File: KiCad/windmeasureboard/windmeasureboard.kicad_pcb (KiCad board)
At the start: 2 copper layers, 101.2 x 73.2 mm, 29 parts, among them J1 ESQ-120-XX-X-D-XX, U1 ESP32-S2-DEVKITC-1, U2 LM1084ISX-5.0_NOPB, U3 INA229AIDGSR, U4 INA229AIDGSR, U5 INA229AIDGSR, U6 INA229AIDGSR, U7 INA229AIDGSR, U8 INA229AIDGSR, U9 INA229AIDGSR

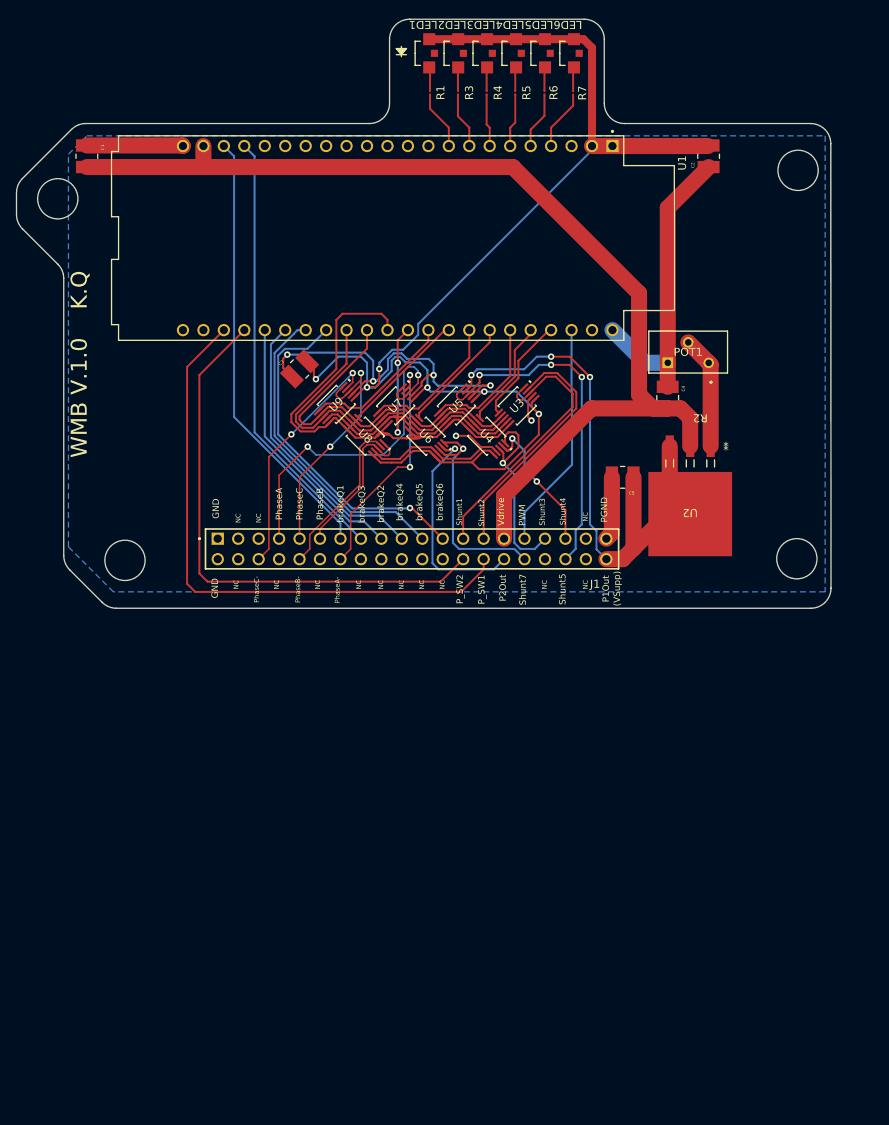
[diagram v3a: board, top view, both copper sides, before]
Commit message: started V2 WMB
fixed PSU issue
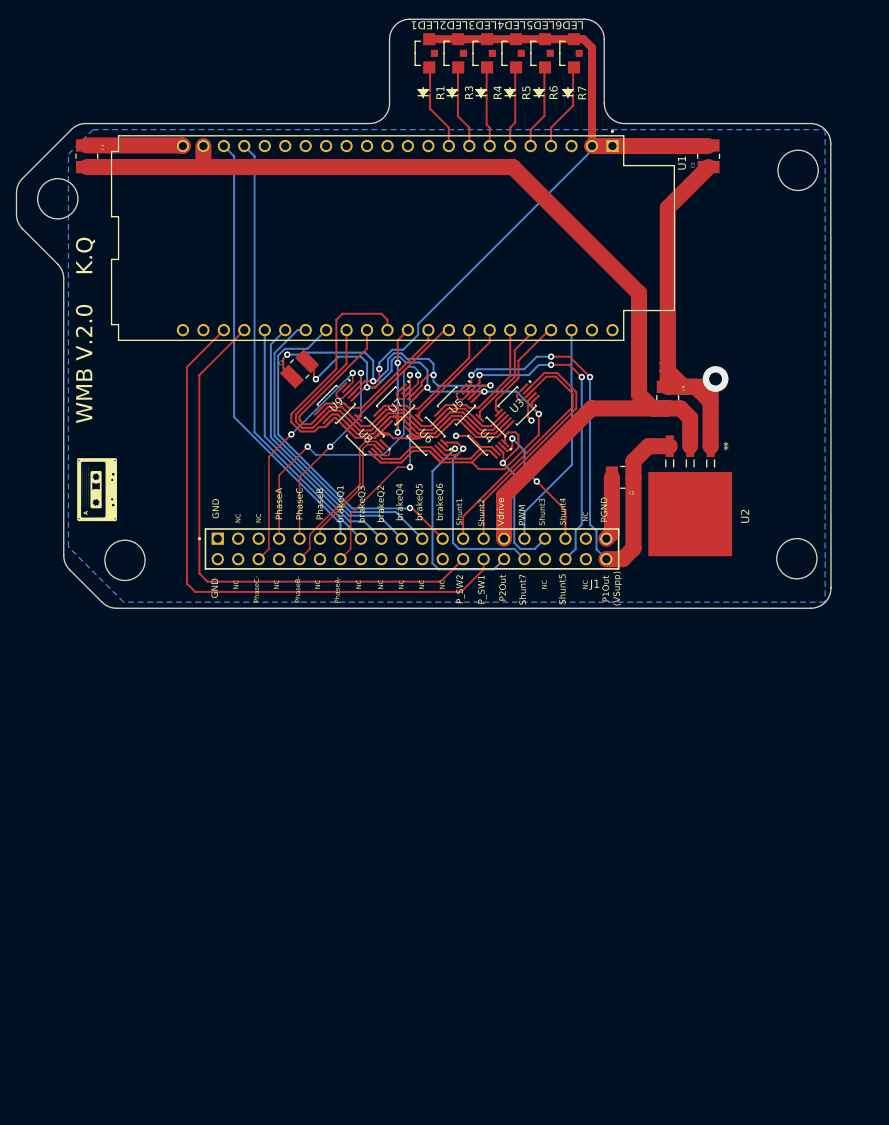
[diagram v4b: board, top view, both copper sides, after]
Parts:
- removed POT1: 3296Y-1-502LF, footprints:POT_3296Y
- removed R2: CRCW04021K00FKED, footprints:RES_CRCW_0402
- added G***: LOGO, LOGO, F.Cu at (91.2, 78.7)
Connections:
- U2 pad 1: Net-(U2-ADJ/GND) -> GND
- U2 pad 4: Shunt6 -> unconnected-(U2-Pad4)
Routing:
- net Net-(U2-ADJ/GND): track 14.0 -> 0.00 mm
- net GND: track 130.7 -> 144.0 mm, vias 6 -> 7
- net Shunt6: track 73.4 -> 62.4 mm
- net unconnected-(U2-Pad4): track 0.00 -> 6.37 mm
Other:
- board text added: "WMB V.2.0 K.Q"
- board text removed: "WMB V.1.0 K.Q"

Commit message: Finished WMB V2.1
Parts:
- removed R7: ERJXGNJ560Y, footprints:ERJXGN_RCD
- added R2: CPA2512E56R0FS-T10, footprints:RESC6332X80N, F.Cu at (134.9, 66.7)
- R1, R3, R4, R5, R6: value ERJXGNJ560Y -> CPA2512E56R0FS-T10; footprint footprints:ERJXGN_RCD -> footprints:RESC6332X80N
- moved C5 45.8 mm to (161.6, 122.7)
- moved C3 45.8 mm to (121.5, 109.3)
- moved C4 45.8 mm to (167.2, 112.8)
- moved G*** 45.8 mm to (96.4, 124.3)
- moved J1 45.8 mm to (135.5, 131.6)
- moved U2 45.8 mm to (170.0, 127.1)
- moved U3 45.8 mm to (148.5, 113.9)
- moved U4 45.8 mm to (144.8, 117.6)
- moved U5 45.8 mm to (141.0, 113.9)
- moved U6 45.8 mm to (137.2, 117.6)
- moved U7 45.8 mm to (133.5, 113.9)
- moved U8 45.8 mm to (129.7, 117.6)
- moved U9 45.8 mm to (126.1, 113.7)
- moved C1 42.2 mm to (95.1, 79.2)
- moved C2 42.2 mm to (172.3, 79.2)
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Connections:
- J1 pad 16: unconnected-(J1-Pad16) -> GEN_CS
- J1 pad 17: Brake_Q3 -> Brake_Q1
- J1 pad 18: unconnected-(J1-Pad18) -> GEN_PWM
- J1 pad 19: Brake_Q2 -> Brake_Q1
- J1 pad 20: unconnected-(J1-Pad20) -> MISO
- J1 pad 21: Brake_Q5 -> Brake_Q4
- J1 pad 22: unconnected-(J1-Pad22) -> SCLK
- J1 pad 23: Brake_Q6 -> Brake_Q4
- J1 pad 24: unconnected-(J1-Pad24) -> MOSI
- J1 pad 37: unconnected-(J1-Pad37) -> V3.3+
- R3 pad 1: LED2 -> LED3
- R3 pad 2: Net-(LED2-Pad1) -> Net-(LED3-Pad1)
- R4 pad 1: LED3 -> LED4
- R4 pad 2: Net-(LED3-Pad1) -> Net-(LED4-Pad1)
- R5 pad 1: LED4 -> LED5
- R5 pad 2: Net-(LED4-Pad1) -> Net-(LED5-Pad1)
- R6 pad 1: LED5 -> LED6
- R6 pad 2: Net-(LED5-Pad1) -> Net-(LED6-Pad1)
- U1 pad J1_16: unconnected-(U1-GPIO10-PadJ1_16) -> GEN_CS
- U1 pad J1_17: unconnected-(U1-GPIO11-PadJ1_17) -> GEN_PWM
- U1 pad J1_19: Brake_Q1 -> unconnected-(U1-GPIO13-PadJ1_19)
- U1 pad J1_20: Brake_Q4 -> unconnected-(U1-GPIO14-PadJ1_20)
- U1 pad J3_11: /measurement chips/MISO -> MISO
- U1 pad J3_12: /measurement chips/SCLK -> SCLK
- U1 pad J3_13: /measurement chips/MOSI -> MOSI
- U1 pad J3_15: Brake_Q6 -> Brake_Q1
- U1 pad J3_16: Brake_Q5 -> Brake_Q4
- U1 pad J3_17: Brake_Q2 -> unconnected-(U1-GPIO33-PadJ3_17)
- U1 pad J3_18: Brake_Q3 -> unconnected-(U1-GPIO21-PadJ3_18)
- U3 pad 2: /measurement chips/MOSI -> MOSI
- U3 pad 4: /measurement chips/MISO -> MISO
- U3 pad 5: /measurement chips/SCLK -> SCLK
- U4 pad 2: /measurement chips/MOSI -> MOSI
- U4 pad 4: /measurement chips/MISO -> MISO
- U4 pad 5: /measurement chips/SCLK -> SCLK
- U5 pad 2: /measurement chips/MOSI -> MOSI
- U5 pad 4: /measurement chips/MISO -> MISO
- U5 pad 5: /measurement chips/SCLK -> SCLK
- U6 pad 2: /measurement chips/MOSI -> MOSI
- U6 pad 4: /measurement chips/MISO -> MISO
- U6 pad 5: /measurement chips/SCLK -> SCLK
- U7 pad 2: /measurement chips/MOSI -> MOSI
- U7 pad 4: /measurement chips/MISO -> MISO
- U7 pad 5: /measurement chips/SCLK -> SCLK
- U8 pad 2: /measurement chips/MOSI -> MOSI
- U8 pad 4: /measurement chips/MISO -> MISO
- U8 pad 5: /measurement chips/SCLK -> SCLK
- U9 pad 2: /measurement chips/MOSI -> MOSI
- U9 pad 4: /measurement chips/MISO -> MISO
- U9 pad 5: /measurement chips/SCLK -> SCLK
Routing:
- net GEN_PWM: track 0.00 -> 94.3 mm, vias 0 -> 1
- net GEN_CS: track 0.00 -> 90.2 mm, vias 0 -> 1
- net SCLK: track 0.00 -> 89.1 mm, vias 0 -> 2
- net MISO: track 0.00 -> 78.7 mm, vias 0 -> 5
- net MOSI: track 0.00 -> 72.8 mm, vias 0 -> 3
- net /measurement chips/SCLK: track 58.9 -> 0.00 mm
- net /measurement chips/MOSI: track 45.9 -> 0.00 mm
- net /measurement chips/MISO: track 43.1 -> 0.00 mm, vias 2 -> 0
- net Brake_Q6: track 42.9 -> 0.00 mm, vias 1 -> 0
- net Brake_Q5: track 39.1 -> 0.00 mm
- net V3.3+: track 174.9 -> 210.9 mm, vias 6 -> 9
- net Brake_Q2: track 35.5 -> 0.00 mm
- net Brake_Q3: track 32.9 -> 0.00 mm
- net GND: track 144.0 -> 173.8 mm, vias 7 -> 15
- net Brake_Q1: track 54.9 -> 44.8 mm, vias 0 -> 1
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- added copper zone on F.Cu, net MISO
- added copper zone on F.Cu, net SCLK
- added copper zone on F.Cu, net V3.3+
- removed copper zone on F.Cu, net /measurement chips/MISO
- removed copper zone on F.Cu, net /measurement chips/SCLK
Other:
- board size 101.2 x 73.2 mm -> 101.2 x 86.5 mm
- board text added: "3.3V"
- board text added: "ALERT GPIO0"
- board text added: "BrakeQ1 GPIO45"
- board text added: "BrakeQ4 GPIO34"
- board text added: "CS1 GPIO1"
- board text added: "CS2 GPIO2"
- board text added: "CS3 GPIO42"
- board text added: "CS4 GPIO41"
- board text added: "CS5 GPIO40"
- board text added: "CS6 GPIO39"
- board text added: "CS7 GPIO38"
- board text added: "GEN_CS GPIO9"
- board text added: "GEN_PWM GPIO10"
- board text added: "LED1 GPIO16"
- board text added: "LED2 GPIO15"
- board text added: "LED3 GPIO7"
- board text added: "LED4 GPIO6"
- board text added: "LED5 GPIO5"
- board text added: "LED6 GPIO4"
- board text added: "MISO"
- board text added: "MISO GPIO37"
- board text added: "MOSI"
- board text added: "MOSI GPIO35"
- board text added: "NC GPIO11"
- board text added: "NC GPIO12"
- board text added: "NC GPIO13"
- board text added: "NC GPIO17"
- board text added: "NC GPIO18"
- board text added: "NC GPIO21"
- board text added: "NC GPIO3"
- board text added: "NC GPIO33"
- board text added: "NC GPIO43"
- board text added: "NC GPIO46 (INPUT ONLY)"
- board text added: "NC GPIO8"
- board text added: "NC GPIO9"
- board text added: "NC RST"
- board text added: "PSW1 GPIO20"
- board text added: "PSW2 GPIO20"
- board text added: "PWM_sig GPIO44"
- board text added: "SCLK"
- board text added: "SCLK GPIO36"
- board text added: "V3.3+"
- board text added: "Vdrive V5.0+"
- board text added: "WMB V.2.1 K.Q"
- board text removed: "WMB V.2.0 K.Q"

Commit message: WMB 2.2 pushed and ordered
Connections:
- U1 pad J3_10: /measurement chips/CS7 -> /measurement chips/CS6
- U1 pad J3_11: MISO -> /measurement chips/CS7
- U1 pad J3_12: SCLK -> MISO
- U1 pad J3_13: MOSI -> SCLK
- U1 pad J3_14: /measurement chips/ALERT -> MOSI
- U1 pad J3_15: Brake_Q1 -> /measurement chips/ALERT
- U1 pad J3_16: Brake_Q4 -> Brake_Q1
- U1 pad J3_17: unconnected-(U1-GPIO33-PadJ3_17) -> Brake_Q4
- U1 pad J3_3: PWM_sig -> unconnected-(U1-U0RXD-PadJ3_3)
- U1 pad J3_4: /measurement chips/CS1 -> PWM_sig
- U1 pad J3_5: /measurement chips/CS2 -> /measurement chips/CS1
- U1 pad J3_6: /measurement chips/CS3 -> /measurement chips/CS2
- U1 pad J3_7: /measurement chips/CS4 -> /measurement chips/CS3
- U1 pad J3_8: /measurement chips/CS5 -> /measurement chips/CS4
- U1 pad J3_9: /measurement chips/CS6 -> /measurement chips/CS5
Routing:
- net unconnected-(U1-GPIO33-PadJ3_17): track 3.41 -> 0.00 mm, vias 1 -> 0
- net unconnected-(U1-U0RXD-PadJ3_3): track 0.00 -> 3.34 mm, vias 0 -> 1
- net Brake_Q1: track 44.8 -> 42.6 mm
- net Brake_Q4: track 57.8 -> 56.0 mm
- net /measurement chips/CS3: track 20.2 -> 21.6 mm
- net PWM_sig: track 31.7 -> 33.1 mm
- net /measurement chips/ALERT: track 50.0 -> 51.3 mm
- net /measurement chips/CS4: track 18.3 -> 17.2 mm
- net /measurement chips/CS7: track 22.9 -> 21.9 mm
- net MOSI: track 72.8 -> 72.1 mm
- net SCLK: track 89.1 -> 89.8 mm
- net /measurement chips/CS1: track 16.5 -> 15.9 mm
- net /measurement chips/CS2: track 17.2 -> 16.7 mm
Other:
- board text added: "ALERT GPIO45"
- board text added: "BRAKEQ1 GPIO34"
- board text added: "BRAKEQ4 GPIO33"
- board text added: "CS1 GPIO2"
- board text added: "CS2 GPIO42"
- board text added: "CS3 GPIO41"
- board text added: "CS4 GPIO40"
- board text added: "CS5 GPIO39"
- board text added: "CS6 GPIO38"
- board text added: "CS7 GPIO37"
- board text added: "INA229"
- board text added: "MISO GPIO36"
- board text added: "MOSI GPIO0"
- board text added: "NC GPIO44"
- board text added: "PWM_sig GPIO1"
- board text added: "SCLK GPIO35"
- board text added: "VIN"
- board text added: "VOUT"
- board text added: "WMB V.2.2 K.Q"
- board text removed: "ALERT GPIO0"
- board text removed: "BrakeQ1 GPIO45"
- board text removed: "BrakeQ4 GPIO34"
- board text removed: "CS1 GPIO1"
- board text removed: "CS2 GPIO2"
- board text removed: "CS3 GPIO42"
- board text removed: "CS4 GPIO41"
- board text removed: "CS5 GPIO40"
- board text removed: "CS6 GPIO39"
- board text removed: "CS7 GPIO38"
- board text removed: "MISO GPIO37"
- board text removed: "MOSI GPIO35"
- board text removed: "NC GPIO33"
- board text removed: "PWM_sig GPIO44"
- board text removed: "SCLK GPIO36"
- board text removed: "WMB V.2.1 K.Q"

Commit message: added some kicad components
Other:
- outline, holes or cut-outs redrawn
- board text added: "WMB V.2.3 K.Q"
- board text removed: "WMB V.2.2 K.Q"
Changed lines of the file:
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@@
   (gr_circle (center 122.65 115.6) (end 122.9 115.6)
     (stroke (width 0.15) (type default)) (fill none) (layer "F.SilkS"))
+  (gr_line (start 91.463377 75.636078) (end 95.943073 71.113257)
+    (stroke (width 0.1) (type default)) (layer "Edge.Cuts"))
   (gr_arc (start 175.5 107.9) (mid 176.914214 108.485786) (end 177.5 109.9)
     (stroke (width 0.1) (type default)) (layer "Edge.Cuts"))
@@
   (gr_line (start 187.516349 128.2) (end 187.516349 136.491625)
     (stroke (width 0.1) (type solid)) (layer "Edge.Cuts"))
+  (gr_arc (start 95.943073 71.113257) (mid 96.594258 70.674778) (end 97.364045 70.52068)
+    (stroke (width 0.1) (type default)) (layer "Edge.Cuts"))
   (gr_line (start 126.684349 62.08668) (end 126.684349 68.02068)
     (stroke (width 0.1) (type solid)) (layer "Edge.Cuts"))
-  (gr_line (start 106.684349 70.52068) (end 92.884349 70.52068)
+  (gr_line (start 106.684349 70.52068) (end 97.364045 70.52068)
     (stroke (width 0.1) (type default)) (layer "Edge.Cuts"))
   (gr_arc (start 179.5 126.2) (mid 178.085786 125.614214) (end 177.5 124.2)
     (stroke (width 0.1) (type default)) (layer "Edge.Cuts"))
-  (gr_line (start 90.884349 81.168716) (end 90.884349 76.22068)
-    (stroke (width 0.1) (type default)) (layer "Edge.Cuts"))
-  (gr_line (start 90.884349 72.52068) (end 90.884349 76.22068)
+  (gr_line (start 90.884349 81.168716) (end 90.884349 77.043501)
     (stroke (width 0.1) (type default)) (layer "Edge.Cuts"))
   (gr_line (start 159.362349 55.54668) (end 159.362349 55.014447)
@@
   (gr_circle (center 99.835845 133.045576) (end 102.335845 133.045576)
     (stroke (width 0.1) (type solid)) (fill none) (layer "Edge.Cuts"))
+  (gr_arc (start 90.884349 77.043501) (mid 91.034762 76.282562) (end 91.463377 75.636078)
+    (stroke (width 0.1) (type default)) (layer "Edge.Cuts"))
   (gr_line (start 86.363452 89.422005) (end 86.363452 86.723613)
     (stroke (width 0.1) (type default)) (layer "Edge.Cuts"))
@@
   (gr_line (start 134.834349 52.514447) (end 156.862349 52.514447)
     (stroke (width 0.1) (type solid)) (layer "Edge.Cuts"))
+  (gr_line (start 170.7 99.74) (end 170.7 96.03)
+    (stroke (width 0.1) (type default)) (layer "Edge.Cuts"))
   (gr_line (start 124.184349 70.52068) (end 106.684349 70.52068)
     (stroke (width 0.1) (type default)) (layer "Edge.Cuts"))
@@
   (gr_line (start 126.692116 55.014447) (end 126.684349 62.08668)
     (stroke (width 0.1) (type default)) (layer "Edge.Cuts"))
-  (gr_line (start 187.493058 81.293625) (end 187.493058 84.2)
+  (gr_line (start 187.493058 81.293625) (end 187.493058 92.03)
     (stroke (width 0.1) (type default)) (layer "Edge.Cuts"))
   (gr_arc (start 185.516349 126.2) (mid 186.930563 126.785786) (end 187.516349 128.2)
@@
   (gr_line locked (start 92.230149 98.031214) (end 92.230149 132.445544)
     (stroke (width 0.1) (type default)) (layer "Edge.Cuts"))
-  (gr_line (start 170.7 105.9) (end 170.7 88.2)
-    (stroke (width 0.1) (type default)) (layer "Edge.Cuts"))
-  (gr_arc (start 187.493058 84.2) (mid 186.907269 85.614199) (end 185.493058 86.2)
-    (stroke (width 0.1) (type default)) (layer "Edge.Cuts"))
-  (gr_circle (center 183.427245 80.928776) (end 185.927245 80.928776)
+  (gr_line (start 170.7 105.9) (end 170.7 99.74)
+    (stroke (width 0.1) (type default)) (layer "Edge.Cuts"))
+  (gr_arc (start 187.493058 92.03) (mid 186.907275 93.444234) (end 185.493058 94.03)
+    (stroke (width 0.1) (type default)) (layer "Edge.Cuts"))
+  (gr_circle (center 183.23 88.09) (end 185.73 88.09)
     (stroke (width 0.1) (type solid)) (fill none) (layer "Edge.Cuts"))
   (gr_line (start 185.516349 126.2) (end 179.5 126.2)
     (stroke (width 0.1) (type default)) (layer "Edge.Cuts"))
-  (gr_line (start 172.7 86.2) (end 185.493058 86.2)
+  (gr_line (start 172.7 94.03) (end 185.493058 94.03)
     (stroke (width 0.1) (type default)) (layer "Edge.Cuts"))
   (gr_arc (start 90.884349 81.168716) (mid 90.795587 81.58056) (end 90.545104 81.919317)
@@
   (gr_arc (start 187.516349 136.491625) (mid 186.784489 138.260074) (end 185.016349 138.99268)
     (stroke (width 0.1) (type default)) (layer "Edge.Cuts"))
-  (gr_arc (start 170.7 88.2) (mid 171.285786 86.785786) (end 172.7 86.2)
+  (gr_arc (start 170.7 96.03) (mid 171.285786 94.615786) (end 172.7 94.03)
     (stroke (width 0.1) (type default)) (layer "Edge.Cuts"))
   (gr_arc (start 92.962382 134.213311) (mid 92.42045 133.402251) (end 92.230149 132.445544)
-    (stroke (width 0.1) (type default)) (layer "Edge.Cuts"))
-  (gr_arc (start 90.884349 72.52068) (mid 91.470135 71.106466) (end 92.884349 70.52068)
     (stroke (width 0.1) (type default)) (layer "Edge.Cuts"))
   (gr_circle (center 91.469891 88.060001) (end 93.969891 88.060001)
@@
     (effects (font (size 0.6 0.6) (thickness 0.12)))
   )
-  (gr_text "WMB V.2.2    K.Q" (at 94.846349 104.44868 90) (layer "F.SilkS")
+  (gr_text "WMB V.2.3    K.Q" (at 94.846349 104.44868 90) (layer "F.SilkS")
     (effects (font (size 2 2) (thickness 0.25)))
   )
